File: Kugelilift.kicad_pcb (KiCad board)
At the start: 2 copper layers, 43 x 43.5 mm, 14 parts, among them J1 I2C, J2 TTL, J4 Stepper, SW1 RESET, SW2 MODE, U1 magnetic-charger, U2 TCRT5000, U3 ULN2003A, U4 esp-01f, U5 UA78M33_TO252

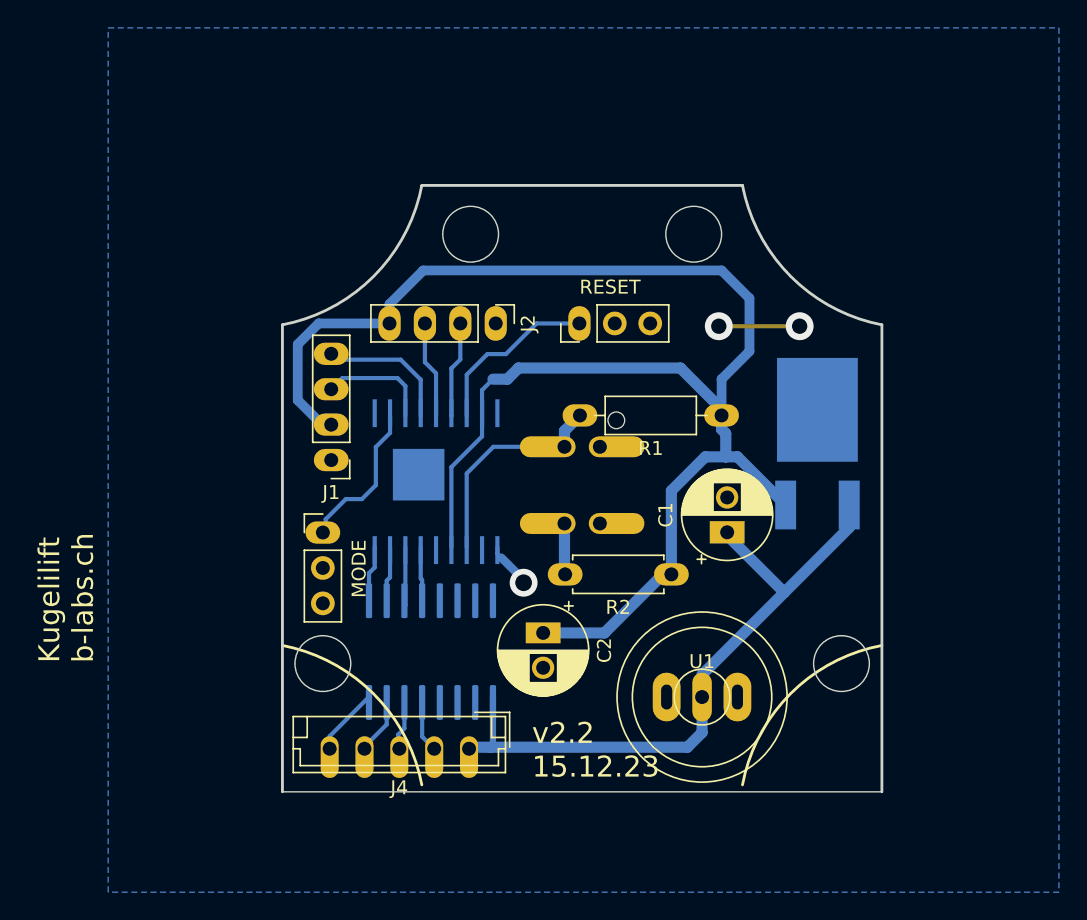
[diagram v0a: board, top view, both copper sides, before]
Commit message: PCB based on ESP01m
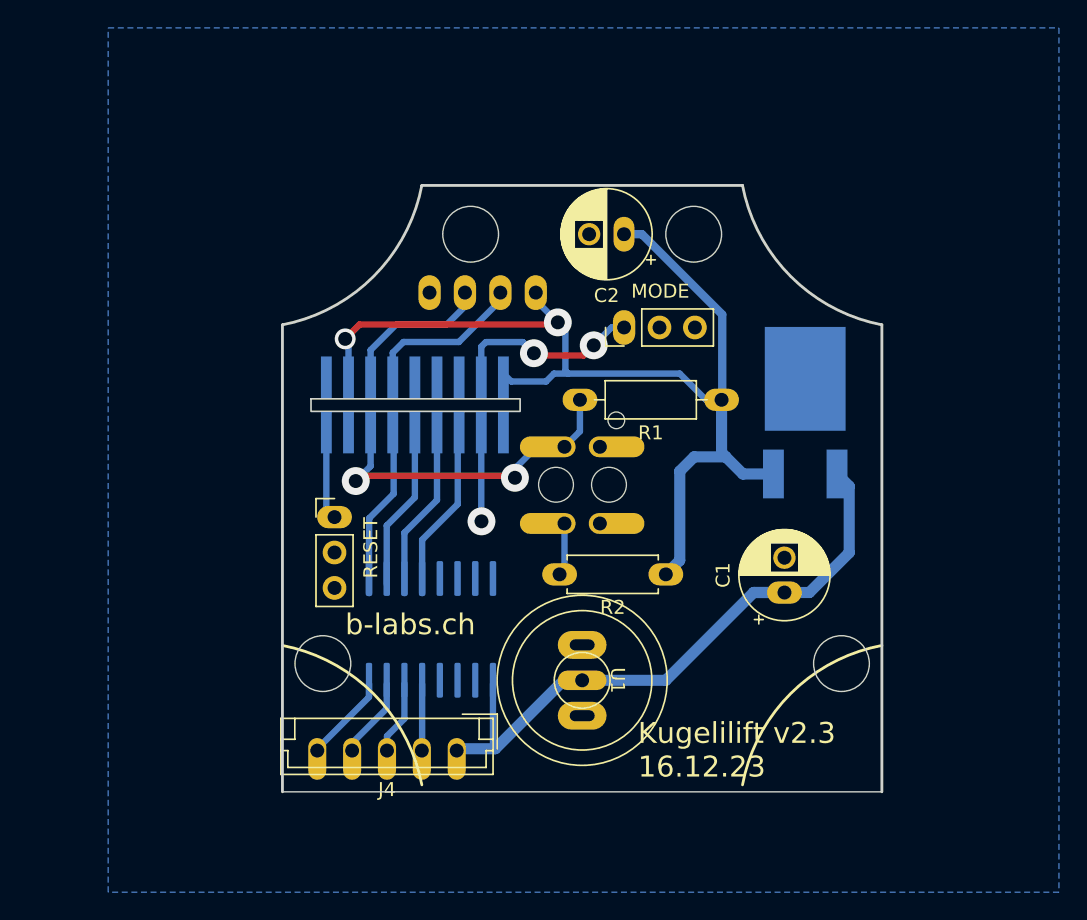
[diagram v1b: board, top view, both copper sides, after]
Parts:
- removed J1: I2C, Connector_PinHeader_2.54mm:PinHeader_1x04_P2.54mm_Vertical
- removed U4: esp-01f, esp-01f:esp-01f
- added U6: esp-01m, esp-01m:esp-01m, B.Cu at (110.0, 72.3)
- J2: moved to B.Cu
- moved C2 29.2 mm to (125.0, 60.0), turned to 180 degrees
- moved SW2 26.1 mm to (125.0, 66.7), turned to 90 degrees
- moved SW1 22.4 mm to (104.2, 80.3), turned to 0 degrees
- moved U1 8.68 mm to (122.0, 92.0), turned to -90 degrees
- moved C1 5.96 mm to (136.5, 85.7)
- moved J2 5.24 mm to (111.1, 64.2)
- moved U5 2.39 mm to (138.0, 73.0)
- moved U3 1.60 mm to (111.2, 88.3)
- moved R1 1.12 mm to (132.0, 71.9)
- moved J4 0.90 mm to (113.0, 97.0)
- moved R2 0.40 mm to (128.0, 84.4)
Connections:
- net /slim-out-1 renamed Net-(J4-Pad5)
- net /slim-out-2 renamed Net-(J4-Pad4)
- net /slim-out-3 renamed Net-(J4-Pad3)
- net /slim-out-4 renamed Net-(J4-Pad2)
- U3 pad 1: Net-(U3-Pad1) -> /in-1
- U3 pad 12: /slim-out-5 -> unconnected-(U3-Pad12)
- U3 pad 3: /in-1 -> /in-3
- U3 pad 4: /in-3 -> /in-4
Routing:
- net +3V3: track 115.0 -> 77.4 mm, vias 0 -> 2
- net /in-4: track 0.00 -> 11.8 mm
- net /SCL: track 9.79 -> 0.00 mm
- net /SDA: track 8.04 -> 0.00 mm
- net Net-(R1-Pad2): track 15.8 -> 23.5 mm, vias 0 -> 2
- net /in-3: track 4.27 -> 11.7 mm
- net /in-2: track 4.33 -> 11.7 mm
- net /in-1: track 4.26 -> 11.5 mm
- net unconnected-(U6-Pad11): track 0.00 -> 6.38 mm, vias 0 -> 1
- net Net-(SW1-Pad1): track 12.6 -> 6.32 mm
- net GND: track 5.80 -> 0.00 mm, vias 2 -> 0
- net Net-(U3-Pad1): track 4.40 -> 0.00 mm
- net RX: track 6.97 -> 11.3 mm
- net TX: track 6.91 -> 11.0 mm
- net Net-(SW2-Pad1): track 10.1 -> 13.5 mm, vias 0 -> 2
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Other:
- board text added: "Kugelilift v2.3 16.12.23"
- board text added: "b-labs.ch"
- board text removed: "Kugelilift b-labs.ch"
- board text removed: "v2.2 15.12.23"
